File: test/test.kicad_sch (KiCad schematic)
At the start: 0 parts

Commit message: Done with the schematic
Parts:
- added A1: RaspberryPi_Pico, Module:RaspberryPi_Pico_Common_THT, symbol MCU_Module:RaspberryPi_Pico
- added D1, D10, D11, D12, D13, D14, D15, D16, D17, D18, D19, D2, D20, D21, D22, D23, D24, D25, D26, D27, D28, D29, D3, D30, D32, D33, D34, D35, D36, D37, D38, D39, D4, D40, D41, D42, D43, D44, D45, D46, D48, D49, D5, D50, D51, D52, D53, D54, D55, D56, D57, D58, D59, D6, D60, D62, D64, D65, D66, D67, D68, D69, D7, D70, D71, D72, D73, D74, D75, D78, D79, D8, D80, D81, D82, D83, D86, D9, D90, D91, D94, D95, D96: 1N4148, Diode_THT:D_DO-35_SOD27_P7.62mm_Horizontal, symbol Diode:1N4148
- added S1, S2, S3, S4, S5, S6, S7: MX_stab, PCM_marbastlib-mx:STAB_MX_P_2u, symbol PCM_marbastlib-mx:MX_stab
- added SW_0, SW_1, SW_2, SW_3, SW_4, SW_5, SW_6, SW_7, SW_8, SW_9, SW_A1, SW_Apostrophe1, SW_ArrowDown1, SW_ArrowLeft1, SW_ArrowRight1, SW_ArrowUp1, SW_B1, SW_C1, SW_CloseBracket1, SW_Colon1, SW_D1, SW_Del1, SW_E1, SW_ESC1, SW_Equals1, SW_F1, SW_F10, SW_F11, SW_F12, SW_F13, SW_F2, SW_F3, SW_F4, SW_F5, SW_F6, SW_F7, SW_F8, SW_F9, SW_FN1, SW_G1, SW_H1, SW_H2, SW_H3, SW_H4, SW_I1, SW_Insert1, SW_J1, SW_K1, SW_L1, SW_M1, SW_Minus1, SW_N1, SW_O1, SW_OpenBracket1, SW_P1, SW_Q1, SW_R1, SW_S1, SW_Slash1, SW_T1, SW_TILDA1, SW_U1, SW_V+1, SW_V-1, SW_V1, SW_VMute1, SW_W1, SW_X1, SW_Y1, SW_Z1, SW_comma1, SW_dot1: SW_Push, PCM_marbastlib-mx:SW_MX_1u, symbol Switch:SW_Push
- added SW_Alt1, SW_CTRL1, SW_PrintScreen1, SW_Super1: SW_Push, PCM_marbastlib-mx:SW_MX_1.25u, symbol Switch:SW_Push
- added SW_BackSpace1, SW_Enter1, SW_Shift1: SW_Push, PCM_marbastlib-mx:SW_MX_1.75u_STP_1.5, symbol Switch:SW_Push
- added SW_Backslash1, SW_CapsLock1: SW_Push, PCM_marbastlib-mx:SW_MX_1.75u, symbol Switch:SW_Push
- added SW_Space1: SW_Push, PCM_marbastlib-mx:SW_MX_1.75u_STP_1.25, symbol Switch:SW_Push
- added SW_TAB1: SW_Push, PCM_marbastlib-mx:SW_MX_1.5u, symbol Switch:SW_Push
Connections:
- new net: D49.2 (A), SW_CapsLock1.2
- new net: D67.2 (A), SW_X1.2
- new net: D59.2 (A), SW_Colon1.2
- new net: D41.2 (A), SW_I1.2
- new net: D29.2 (A), SW_Equals1.2
- new net: D34.2 (A), SW_Q1.2
- new net: D64.2 (A), SW_H3.2
- new net: D8.2 (A), SW_F7.2
- new net: D20.2 (A), SW_3.2
- new net: D65.2 (A), SW_Shift1.2
- new net: D22.2 (A), SW_5.2
- new net: D14.2 (A), SW_VMute1.2
- new net: D57.2 (A), SW_K1.2
- new net: D13.2 (A), SW_F12.2
- new net: D66.2 (A), SW_Z1.2
- new net: D12.2 (A), SW_F11.2
- new net: D95.2 (A), SW_ArrowDown1.2
- new net: D79.2 (A), SW_ArrowUp1.2
- new net: D5.2 (A), SW_F4.2
- new net: D69.2 (A), SW_V1.2
- new net: D1.2 (A), SW_ESC1.2
- new net: D24.2 (A), SW_7.2
- new net: D11.2 (A), SW_F10.2
- new net: D86.2 (A), SW_Space1.2
- new net: D26.2 (A), SW_9.2
- new net: D75.2 (A), SW_Slash1.2
- new net: D70.2 (A), SW_B1.2
- new net: D25.2 (A), SW_8.2
- new net: D78.2 (A), SW_H1.2
- new net: D81.2 (A), SW_CTRL1.2
- new net: D60.2 (A), SW_Apostrophe1.2
- new net: D4.2 (A), SW_F3.2
- new net: D10.2 (A), SW_F9.2
- new net: D42.2 (A), SW_O1.2
- new net: D43.2 (A), SW_P1.2
- new net: D58.2 (A), SW_L1.2
- new net: D56.2 (A), SW_J1.2
- new net: D48.2 (A), SW_Insert1.2
- new net: D55.2 (A), SW_H4.2
- new net: D7.2 (A), SW_F6.2
- new net: D33.2 (A), SW_TAB1.2
- new net: D91.2 (A), SW_PrintScreen1.2
- new net: D52.2 (A), SW_D1.2
- new net: D28.2 (A), SW_Minus1.2
- new net: D44.2 (A), SW_OpenBracket1.2
- new net: D21.2 (A), SW_4.2
- new net: D53.2 (A), SW_F13.2
- new net: D51.2 (A), SW_S1.2
- new net: D71.2 (A), SW_N1.2
- new net: D80.2 (A), SW_H2.2
- new net: D17.2 (A), SW_TILDA1.2
- new net: D74.2 (A), SW_dot1.2
- new net: D16.2 (A), SW_V+1.2
- new net: D82.2 (A), SW_Super1.2
- new net: D83.2 (A), SW_Alt1.2
- new net: D39.2 (A), SW_Y1.2
- new net: D90.2 (A), SW_FN1.2
- new net: D40.2 (A), SW_U1.2
- new net: D36.2 (A), SW_E1.2
- new net: D94.2 (A), SW_ArrowLeft1.2
- new net: D45.2 (A), SW_CloseBracket1.2
- new net: D2.2 (A), SW_F1.2
- new net: D6.2 (A), SW_F5.2
- new net: D30.2 (A), SW_BackSpace1.2
- new net: D37.2 (A), SW_R1.2
- new net: A1.13 (GND), A1.18 (GND), A1.23 (GND), A1.28 (GND), A1.3 (GND), A1.38 (GND), A1.8 (GND)
- new net: D72.2 (A), SW_M1.2
- new net: D32.2 (A), SW_Del1.2
- new net: D46.2 (A), SW_Backslash1.2
- new net: D15.2 (A), SW_V-1.2
- new net: D54.2 (A), SW_G1.2
- new net: D35.2 (A), SW_W1.2
- new net: D9.2 (A), SW_F8.2
- new net: D62.2 (A), SW_Enter1.2
- new net: D23.2 (A), SW_6.2
- new net: D27.2 (A), SW_0.2
- new net: D68.2 (A), SW_C1.2
- new net: D50.2 (A), SW_A1.2
- new net: D73.2 (A), SW_comma1.2
- new net: D19.2 (A), SW_2.2
- new net: D18.2 (A), SW_1.2
- new net: D38.2 (A), SW_T1.2
- new net: D96.2 (A), SW_ArrowRight1.2
- new net: D3.2 (A), SW_F2.2
- new net Col1: A1.9 (GPIO6), SW_CTRL1.1, SW_CapsLock1.1, SW_ESC1.1, SW_Shift1.1, SW_TAB1.1, SW_TILDA1.1
- new net Col10: A1.20 (GPIO15), SW_9.1, SW_F9.1, SW_FN1.1, SW_L1.1, SW_O1.1, SW_dot1.1
- new net Col11: A1.21 (GPIO16), SW_0.1, SW_Colon1.1, SW_F10.1, SW_P1.1, SW_PrintScreen1.1, SW_Slash1.1
- new net Col12: A1.22 (GPIO17), SW_Apostrophe1.1, SW_F11.1, SW_Minus1.1, SW_OpenBracket1.1
- new net Col13: A1.24 (GPIO18), SW_CloseBracket1.1, SW_Equals1.1, SW_F12.1
- new net Col14: A1.25 (GPIO19), SW_ArrowLeft1.1, SW_BackSpace1.1, SW_Backslash1.1, SW_Enter1.1, SW_H1.1, SW_VMute1.1
- new net Col15: A1.26 (GPIO20), SW_ArrowDown1.1, SW_ArrowUp1.1, SW_V-1.1
- new net Col16: A1.27 (GPIO21), SW_ArrowRight1.1, SW_Del1.1, SW_H2.1, SW_H3.1, SW_Insert1.1, SW_V+1.1
- new net Col2: A1.10 (GPIO7), SW_1.1, SW_A1.1, SW_F1.1, SW_Q1.1, SW_Super1.1, SW_Z1.1
- new net Col3: A1.11 (GPIO8), SW_2.1, SW_Alt1.1, SW_F2.1, SW_S1.1, SW_W1.1, SW_X1.1
- new net Col4: A1.12 (GPIO9), SW_3.1, SW_C1.1, SW_D1.1, SW_E1.1, SW_F3.1
- new net Col5: A1.14 (GPIO10), SW_4.1, SW_F13.1, SW_F4.1, SW_R1.1, SW_V1.1
- new net Col6: A1.15 (GPIO11), SW_5.1, SW_B1.1, SW_F5.1, SW_G1.1, SW_Space1.1, SW_T1.1
- new net Col7: A1.16 (GPIO12), SW_6.1, SW_F6.1, SW_H4.1, SW_N1.1, SW_Y1.1
- new net Col8: A1.17 (GPIO13), SW_7.1, SW_F7.1, SW_J1.1, SW_M1.1, SW_U1.1
- new net Col9: A1.19 (GPIO14), SW_8.1, SW_F8.1, SW_I1.1, SW_K1.1, SW_comma1.1
- new net Row1: A1.1 (GPIO0), D1.1 (K), D10.1 (K), D11.1 (K), D12.1 (K), D13.1 (K), D14.1 (K), D15.1 (K), D16.1 (K), D2.1 (K), D3.1 (K), D4.1 (K), D5.1 (K), D6.1 (K), D7.1 (K), D8.1 (K), D9.1 (K)
- new net Row2: A1.2 (GPIO1), D17.1 (K), D18.1 (K), D19.1 (K), D20.1 (K), D21.1 (K), D22.1 (K), D23.1 (K), D24.1 (K), D25.1 (K), D26.1 (K), D27.1 (K), D28.1 (K), D29.1 (K), D30.1 (K), D32.1 (K)
- new net Row3: A1.4 (GPIO2), D33.1 (K), D34.1 (K), D35.1 (K), D36.1 (K), D37.1 (K), D38.1 (K), D39.1 (K), D40.1 (K), D41.1 (K), D42.1 (K), D43.1 (K), D44.1 (K), D45.1 (K), D46.1 (K), D48.1 (K)
- new net Row4: A1.5 (GPIO3), D49.1 (K), D50.1 (K), D51.1 (K), D52.1 (K), D53.1 (K), D54.1 (K), D55.1 (K), D56.1 (K), D57.1 (K), D58.1 (K), D59.1 (K), D60.1 (K), D62.1 (K), D64.1 (K)
- new net Row5: A1.6 (GPIO4), D65.1 (K), D66.1 (K), D67.1 (K), D68.1 (K), D69.1 (K), D70.1 (K), D71.1 (K), D72.1 (K), D73.1 (K), D74.1 (K), D75.1 (K), D78.1 (K), D79.1 (K), D80.1 (K)
- new net Row6: A1.7 (GPIO5), D81.1 (K), D82.1 (K), D83.1 (K), D86.1 (K), D90.1 (K), D91.1 (K), D94.1 (K), D95.1 (K), D96.1 (K)

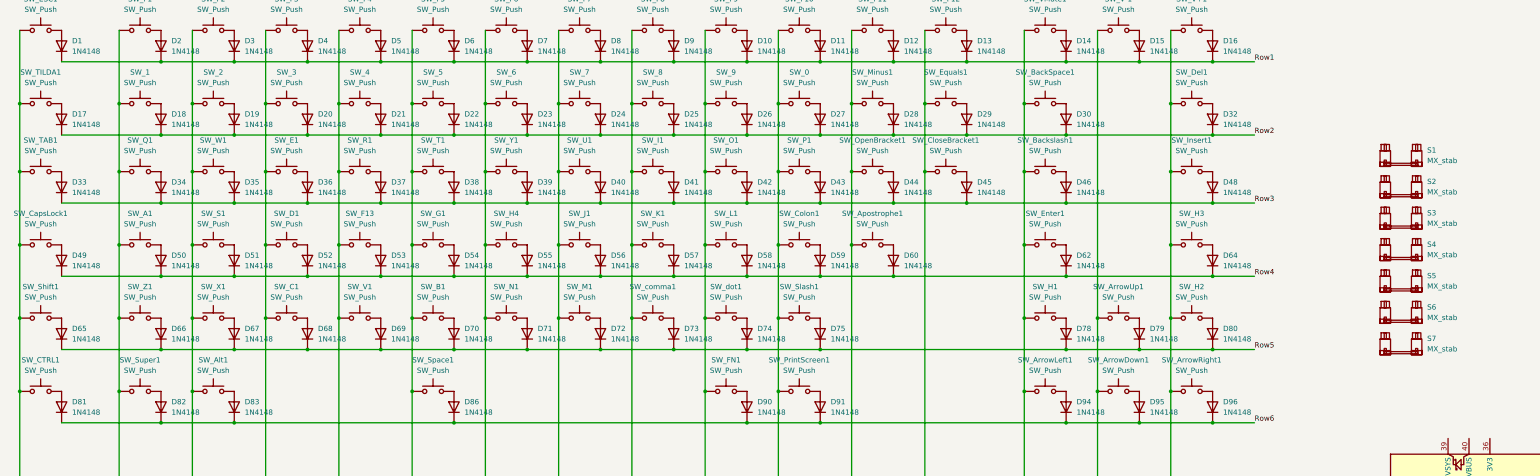
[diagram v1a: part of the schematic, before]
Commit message: added layout using keyboard-layout-editor
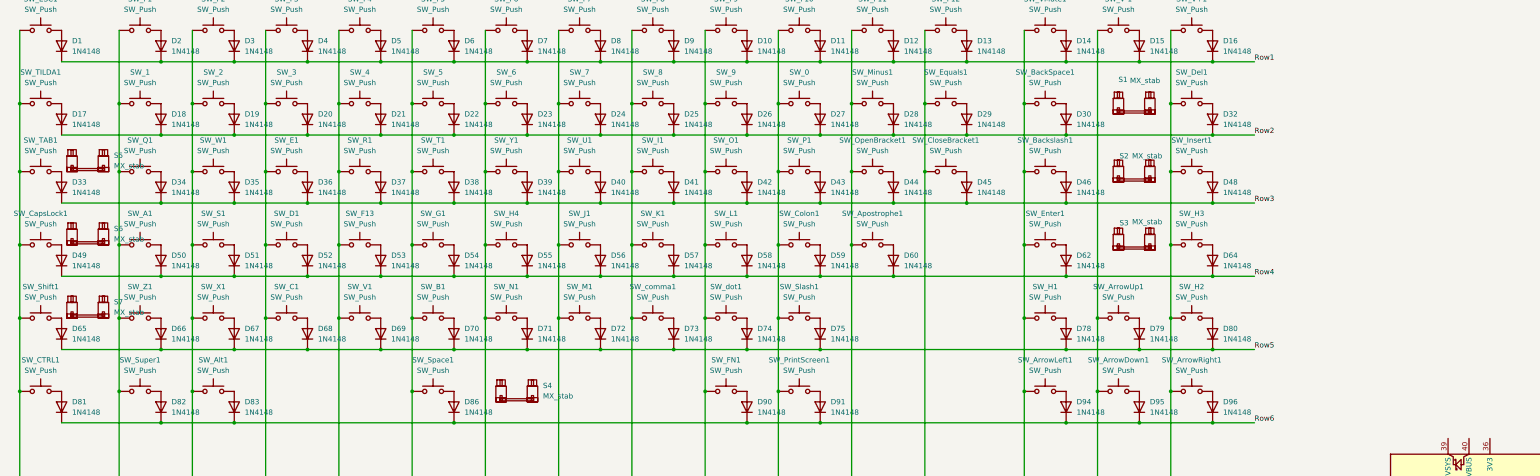
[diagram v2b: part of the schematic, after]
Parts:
- S1, S2, S3, S4, S5, S6, S7: footprint PCM_marbastlib-mx:STAB_MX_P_2u -> PCM_marbastlib-mx:SW_MX_1u
- SW_Alt1, SW_CTRL1, SW_PrintScreen1, SW_Super1: footprint PCM_marbastlib-mx:SW_MX_1.25u -> PCM_marbastlib-mx:SW_MX_1u
- SW_BackSpace1, SW_Enter1, SW_Shift1: footprint PCM_marbastlib-mx:SW_MX_1.75u_STP_1.5 -> PCM_marbastlib-mx:SW_MX_1u
- SW_Backslash1, SW_CapsLock1: footprint PCM_marbastlib-mx:SW_MX_1.75u -> PCM_marbastlib-mx:SW_MX_1u
- SW_Space1: footprint PCM_marbastlib-mx:SW_MX_1.75u_STP_1.25 -> PCM_marbastlib-mx:SW_MX_1u
- SW_TAB1: footprint PCM_marbastlib-mx:SW_MX_1.5u -> PCM_marbastlib-mx:SW_MX_1u
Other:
- moved on the sheet: S1, S2, S3, S4, S5, S6, S7
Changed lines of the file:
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@@
 	(symbol
 		(lib_id "PCM_marbastlib-mx:MX_stab")
-		(at 355.6 107.95 0)
+		(at 290.83 104.14 0)
 		(unit 1)
 		(body_style 1)
@@
 		(in_pos_files yes)
 		(dnp no)
-		(fields_autoplaced yes)
 		(property "Reference" "S2"
-			(at 361.95 106.5529 0)
+			(at 287.274 100.33 0)
 			(show_name no)
 			(do_not_autoplace no)
@@
 		)
 		(property "Value" "MX_stab"
-			(at 361.95 109.0929 0)
+			(at 290.322 100.33 0)
 			(show_name no)
 			(do_not_autoplace no)
@@
 			)
 		)
-		(property "Footprint" "PCM_marbastlib-mx:STAB_MX_P_2u"
-			(at 355.6 107.95 0)
+		(property "Footprint" "PCM_marbastlib-mx:SW_MX_1u"
+			(at 290.83 104.14 0)
 			(hide yes)
 			(show_name no)
@@
 		)
 		(property "Datasheet" ""
-			(at 355.6 107.95 0)
+			(at 290.83 104.14 0)
 			(hide yes)
 			(show_name no)
@@
 		)
 		(property "Description" "Cherry MX-style stabilizer"
-			(at 355.6 107.95 0)
+			(at 290.83 104.14 0)
 			(hide yes)
 			(show_name no)
@@
 			)
 		)
-		(property "Footprint" "PCM_marbastlib-mx:SW_MX_1.75u_STP_1.25"
+		(property "Footprint" "PCM_marbastlib-mx:SW_MX_1u"
 			(at 120.65 152.4 0)
 			(hide yes)
@@
 	(symbol
 		(lib_id "PCM_marbastlib-mx:MX_stab")
-		(at 355.6 100.33 0)
+		(at 290.83 87.63 0)
 		(unit 1)
 		(body_style 1)
@@
 		(in_pos_files yes)
 		(dnp no)
-		(fields_autoplaced yes)
 		(property "Reference" "S1"
-			(at 361.95 98.9329 0)
+			(at 287.02 81.788 0)
 			(show_name no)
 			(do_not_autoplace no)
@@
 		)
 		(property "Value" "MX_stab"
-			(at 361.95 101.4729 0)
+			(at 289.814 82.042 0)
 			(show_name no)
 			(do_not_autoplace no)
@@
 			)
 		)
-		(property "Footprint" "PCM_marbastlib-mx:STAB_MX_P_2u"
-			(at 355.6 100.33 0)
+		(property "Footprint" "PCM_marbastlib-mx:SW_MX_1u"
+			(at 290.83 87.63 0)
 			(hide yes)
 			(show_name no)
@@
 		)
 		(property "Datasheet" ""
-			(at 355.6 100.33 0)
+			(at 290.83 87.63 0)
 			(hide yes)
 			(show_name no)
@@
 		)
 		(property "Description" "Cherry MX-style stabilizer"
-			(at 355.6 100.33 0)
+			(at 290.83 87.63 0)
 			(hide yes)
 			(show_name no)
@@
 			)
 		)
-		(property "Footprint" "PCM_marbastlib-mx:SW_MX_1.75u"
+		(property "Footprint" "PCM_marbastlib-mx:SW_MX_1u"
 			(at 25.4 116.84 0)
 			(hide yes)
@@
 			)
 		)
-		(property "Footprint" "PCM_marbastlib-mx:SW_MX_1.5u"
+		(property "Footprint" "PCM_marbastlib-mx:SW_MX_1u"
 			(at 25.4 99.06 0)
 			(hide yes)
@@
 	(symbol
 		(lib_id "PCM_marbastlib-mx:MX_stab")
-		(at 355.6 138.43 0)
+		(at 36.83 119.38 0)
 		(unit 1)
 		(body_style 1)
@@
 		(fields_autoplaced yes)
 		(property "Reference" "S6"
-			(at 361.95 137.0329 0)
+			(at 43.18 117.9829 0)
 			(show_name no)
 			(do_not_autoplace no)
@@
 		)
 		(property "Value" "MX_stab"
-			(at 361.95 139.5729 0)
+			(at 43.18 120.5229 0)
 			(show_name no)
 			(do_not_autoplace no)
@@
 			)
 		)
-		(property "Footprint" "PCM_marbastlib-mx:STAB_MX_P_2u"
-			(at 355.6 138.43 0)
+		(property "Footprint" "PCM_marbastlib-mx:SW_MX_1u"
+			(at 36.83 119.38 0)
 			(hide yes)
 			(show_name no)
@@
 		)
 		(property "Datasheet" ""
-			(at 355.6 138.43 0)
+			(at 36.83 119.38 0)
 			(hide yes)
 			(show_name no)
@@
 		)
 		(property "Description" "Cherry MX-style stabilizer"
-			(at 355.6 138.43 0)
+			(at 36.83 119.38 0)
 			(hide yes)
 			(show_name no)
@@
 	(symbol
 		(lib_id "PCM_marbastlib-mx:MX_stab")
-		(at 355.6 130.81 0)
+		(at 36.83 101.6 0)
 		(unit 1)
 		(body_style 1)
@@
 		(fields_autoplaced yes)
 		(property "Reference" "S5"
-			(at 361.95 129.4129 0)
+			(at 43.18 100.2029 0)
 			(show_name no)
 			(do_not_autoplace no)
@@
 		)
 		(property "Value" "MX_stab"
-			(at 361.95 131.9529 0)
+			(at 43.18 102.7429 0)
 			(show_name no)
 			(do_not_autoplace no)
@@
 			)
 		)
-		(property "Footprint" "PCM_marbastlib-mx:STAB_MX_P_2u"
-			(at 355.6 130.81 0)
+		(property "Footprint" "PCM_marbastlib-mx:SW_MX_1u"
+			(at 36.83 101.6 0)
 			(hide yes)
 			(show_name no)
@@
 		)
 		(property "Datasheet" ""
-			(at 355.6 130.81 0)
+			(at 36.83 101.6 0)
 			(hide yes)
 			(show_name no)
@@
 		)
 		(property "Description" "Cherry MX-style stabilizer"
-			(at 355.6 130.81 0)
+			(at 36.83 101.6 0)
 			(hide yes)
 			(show_name no)
@@
 	(symbol
 		(lib_id "PCM_marbastlib-mx:MX_stab")
-		(at 355.6 115.57 0)
+		(at 290.83 120.65 0)
 		(unit 1)
 		(body_style 1)
@@
 		(in_pos_files yes)
 		(dnp no)
-		(fields_autoplaced yes)
 		(property "Reference" "S3"
-			(at 361.95 114.1729 0)
+			(at 287.274 116.586 0)
 			(show_name no)
 			(do_not_autoplace no)
@@
 		)
 		(property "Value" "MX_stab"
-			(at 361.95 116.7129 0)
+			(at 290.322 116.332 0)
 			(show_name no)
 			(do_not_autoplace no)
@@
 			)
 		)
-		(property "Footprint" "PCM_marbastlib-mx:STAB_MX_P_2u"
-			(at 355.6 115.57 0)
+		(property "Footprint" "PCM_marbastlib-mx:SW_MX_1u"
+			(at 290.83 120.65 0)
 			(hide yes)
 			(show_name no)
@@
 		)
 		(property "Datasheet" ""
-			(at 355.6 115.57 0)
+			(at 290.83 120.65 0)
 			(hide yes)
 			(show_name no)
@@
 		)
 		(property "Description" "Cherry MX-style stabilizer"
-			(at 355.6 115.57 0)
+			(at 290.83 120.65 0)
 			(hide yes)
 			(show_name no)
@@
 			)
 		)
-		(property "Footprint" "PCM_marbastlib-mx:SW_MX_1.75u"
+		(property "Footprint" "PCM_marbastlib-mx:SW_MX_1u"
 			(at 269.24 99.06 0)
 			(hide yes)
@@
 			)
 		)
-		(property "Footprint" "PCM_marbastlib-mx:SW_MX_1.25u"
+		(property "Footprint" "PCM_marbastlib-mx:SW_MX_1u"
 			(at 209.55 152.4 0)
 			(hide yes)
@@
 			)
 		)
-		(property "Footprint" "PCM_marbastlib-mx:SW_MX_1.75u_STP_1.5"
+		(property "Footprint" "PCM_marbastlib-mx:SW_MX_1u"
 			(at 25.4 134.62 0)
 			(hide yes)
@@
 			)
 		)
-		(property "Footprint" "PCM_marbastlib-mx:SW_MX_1.25u"
+		(property "Footprint" "PCM_marbastlib-mx:SW_MX_1u"
 			(at 49.53 152.4 0)
 			(hide yes)
@@
 	(symbol
 		(lib_id "PCM_marbastlib-mx:MX_stab")
-		(at 355.6 146.05 0)
+		(at 36.83 137.16 0)
 		(unit 1)
 		(body_style 1)
@@
 		(fields_autoplaced yes)
 		(property "Reference" "S7"
-			(at 361.95 144.6529 0)
+			(at 43.18 135.7629 0)
 			(show_name no)
 			(do_not_autoplace no)
@@
 		)
 		(property "Value" "MX_stab"
-			(at 361.95 147.1929 0)
+			(at 43.18 138.3029 0)
 			(show_name no)
 			(do_not_autoplace no)
@@
 			)
 		)
-		(property "Footprint" "PCM_marbastlib-mx:STAB_MX_P_2u"
-			(at 355.6 146.05 0)
+		(property "Footprint" "PCM_marbastlib-mx:SW_MX_1u"
+			(at 36.83 137.16 0)
 			(hide yes)
 			(show_name no)
@@
 		)
 		(property "Datasheet" ""
-			(at 355.6 146.05 0)
+			(at 36.83 137.16 0)
 			(hide yes)
 			(show_name no)
@@
 		)
 		(property "Description" "Cherry MX-style stabilizer"
-			(at 355.6 146.05 0)
+			(at 36.83 137.16 0)
 			(hide yes)
 			(show_name no)
@@
 	(symbol
 		(lib_id "PCM_marbastlib-mx:MX_stab")
-		(at 355.6 123.19 0)
+		(at 140.97 157.48 0)
 		(unit 1)
 		(body_style 1)
@@
 		(fields_autoplaced yes)
 		(property "Reference" "S4"
-			(at 361.95 121.7929 0)
+			(at 147.32 156.0829 0)
 			(show_name no)
 			(do_not_autoplace no)
@@
 		)
 		(property "Value" "MX_stab"
-			(at 361.95 124.3329 0)
+			(at 147.32 158.6229 0)
 			(show_name no)
 			(do_not_autoplace no)
@@
 			)
 		)
-		(property "Footprint" "PCM_marbastlib-mx:STAB_MX_P_2u"
-			(at 355.6 123.19 0)
+		(property "Footprint" "PCM_marbastlib-mx:SW_MX_1u"
+			(at 140.97 157.48 0)
 			(hide yes)
 			(show_name no)
@@
 		)
 		(property "Datasheet" ""
-			(at 355.6 123.19 0)
+			(at 140.97 157.48 0)
 			(hide yes)
 			(show_name no)
@@
 		)
 		(property "Description" "Cherry MX-style stabilizer"
-			(at 355.6 123.19 0)
+			(at 140.97 157.48 0)
 			(hide yes)
 			(show_name no)
@@
 			)
 		)
-		(property "Footprint" "PCM_marbastlib-mx:SW_MX_1.75u_STP_1.5"
+		(property "Footprint" "PCM_marbastlib-mx:SW_MX_1u"
 			(at 269.24 82.55 0)
 			(hide yes)
@@
 			)
 		)
-		(property "Footprint" "PCM_marbastlib-mx:SW_MX_1.25u"
+		(property "Footprint" "PCM_marbastlib-mx:SW_MX_1u"
 			(at 67.31 152.4 0)
 			(hide yes)
@@
 			)
 		)
-		(property "Footprint" "PCM_marbastlib-mx:SW_MX_1.75u_STP_1.5"
+		(property "Footprint" "PCM_marbastlib-mx:SW_MX_1u"
 			(at 269.24 116.84 0)
 			(hide yes)
@@
 			)
 		)
-		(property "Footprint" "PCM_marbastlib-mx:SW_MX_1.25u"
+		(property "Footprint" "PCM_marbastlib-mx:SW_MX_1u"
 			(at 25.4 152.4 0)
 			(hide yes)

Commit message: Started pcb editor
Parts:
- removed S2, S5, S6: MX_stab, PCM_marbastlib-mx:SW_MX_1u, symbol PCM_marbastlib-mx:MX_stab
- added D81: 1N4148, Diode_THT:D_DO-35_SOD27_P7.62mm_Horizontal, symbol Diode:1N4148
- added SW81: SW_Push, PCM_marbastlib-mx:SW_MX_1u, symbol Switch:SW_Push
- S1: footprint PCM_marbastlib-mx:SW_MX_1u -> PCM_marbastlib-mx:STAB_MX_2u
- S2: renamed from S3; footprint PCM_marbastlib-mx:SW_MX_1u -> PCM_marbastlib-mx:STAB_MX_2.25u
- S3: renamed from S7; footprint PCM_marbastlib-mx:SW_MX_1u -> PCM_marbastlib-mx:STAB_MX_2.25u
- S4: footprint PCM_marbastlib-mx:SW_MX_1u -> PCM_marbastlib-mx:STAB_MX_5u
- renumbered D32 to D31, D33 to D32, D34 to D33, D35 to D34, D36 to D35, D37 to D36, D38 to D37, D39 to D38, D40 to D39, D41 to D40, D42 to D41, D43 to D42, D44 to D43, D45 to D44, D46 to D45, D48 to D46, D49 to D47, D50 to D48, D51 to D49, D52 to D50, D53 to D51, D54 to D52, D55 to D53, D56 to D54, D57 to D55, D58 to D56, D59 to D57, D60 to D58, D62 to D59, D64 to D60, D65 to D61, D66 to D62, D67 to D63, D68 to D64, D69 to D65, D70 to D66, D71 to D67, D72 to D68, D73 to D69, D74 to D70, D75 to D71, D78 to D72, D79 to D73, D80 to D74, D81 to D75, D82 to D76, D83 to D77, D86 to D78, D90 to D79, D91 to D80, D94 to D82, D95 to D83, D96 to D84, SW_ESC1 to SW1, SW_F9 to SW10, SW_F10 to SW11, SW_F11 to SW12, SW_F12 to SW13, SW_VMute1 to SW14, SW_V-1 to SW15, SW_V+1 to SW16, SW_TILDA1 to SW17, SW_1 to SW18, SW_2 to SW19, SW_F1 to SW2, SW_3 to SW20, SW_4 to SW21, SW_5 to SW22, SW_6 to SW23, SW_7 to SW24, SW_8 to SW25, SW_9 to SW26, SW_0 to SW27, SW_Minus1 to SW28, SW_Equals1 to SW29, SW_F2 to SW3, SW_BackSpace1 to SW30, SW_Del1 to SW31, SW_TAB1 to SW32, SW_Q1 to SW33, SW_W1 to SW34, SW_E1 to SW35, SW_R1 to SW36, SW_T1 to SW37, SW_Y1 to SW38, SW_U1 to SW39, SW_F3 to SW4, SW_I1 to SW40, SW_O1 to SW41, SW_P1 to SW42, SW_OpenBracket1 to SW43, SW_CloseBracket1 to SW44, SW_Backslash1 to SW45, SW_Insert1 to SW46, SW_CapsLock1 to SW47, SW_A1 to SW48, SW_S1 to SW49, SW_F4 to SW5, SW_D1 to SW50, SW_F13 to SW51, SW_G1 to SW52, SW_H4 to SW53, SW_J1 to SW54, SW_K1 to SW55, SW_L1 to SW56, SW_Colon1 to SW57, SW_Apostrophe1 to SW58, SW_Enter1 to SW59, SW_F5 to SW6, SW_H3 to SW60, SW_Shift1 to SW61, SW_Z1 to SW62, SW_X1 to SW63, SW_C1 to SW64, SW_V1 to SW65, SW_B1 to SW66, SW_N1 to SW67, SW_M1 to SW68, SW_comma1 to SW69, SW_F6 to SW7, SW_dot1 to SW70, SW_Slash1 to SW71, SW_H1 to SW72, SW_ArrowUp1 to SW73, SW_H2 to SW74, SW_CTRL1 to SW75, SW_Super1 to SW76, SW_Alt1 to SW77, SW_Space1 to SW78, SW_FN1 to SW79, SW_F7 to SW8, SW_PrintScreen1 to SW80, SW_ArrowLeft1 to SW82, SW_ArrowDown1 to SW83, SW_ArrowRight1 to SW84, SW_F8 to SW9
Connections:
- net Col12: now also SW81.1
- net Row6: now also D81.1 (K)
- new net: D81.2 (A), SW81.2

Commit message: Finished the pcb design
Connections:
- net Col1: now also A1.1 (GPIO0); no longer A1.9 (GPIO6)
- net Col10: now also A1.12 (GPIO9), SW80.1; no longer A1.20 (GPIO15), SW79.1
- net Col11: now also A1.14 (GPIO10), SW81.1; no longer A1.21 (GPIO16), SW80.1
- net Col12: now also A1.15 (GPIO11); no longer A1.22 (GPIO17), SW81.1
- net Col13: now also A1.16 (GPIO12); no longer A1.24 (GPIO18)
- net Col14: now also A1.17 (GPIO13); no longer A1.25 (GPIO19)
- net Col15: now also A1.19 (GPIO14); no longer A1.26 (GPIO20)
- net Col16: now also A1.20 (GPIO15); no longer A1.27 (GPIO21)
- net Col2: now also A1.2 (GPIO1); no longer A1.10 (GPIO7)
- net Col3: now also A1.4 (GPIO2); no longer A1.11 (GPIO8)
- net Col4: now also A1.5 (GPIO3); no longer A1.12 (GPIO9)
- net Col5: now also A1.6 (GPIO4); no longer A1.14 (GPIO10)
- net Col6: now also A1.7 (GPIO5); no longer A1.15 (GPIO11)
- net Col7: now also A1.9 (GPIO6); no longer A1.16 (GPIO12)
- net Col8: now also A1.10 (GPIO7); no longer A1.17 (GPIO13)
- net Col9: now also A1.11 (GPIO8), SW79.1; no longer A1.19 (GPIO14)
- net Row1: now also A1.22 (GPIO17); no longer A1.1 (GPIO0)
- net Row2: now also A1.24 (GPIO18); no longer A1.2 (GPIO1)
- net Row3: now also A1.25 (GPIO19); no longer A1.4 (GPIO2)
- net Row4: now also A1.26 (GPIO20); no longer A1.5 (GPIO3)
- net Row5: now also A1.27 (GPIO21); no longer A1.6 (GPIO4)
- net Row6: now also A1.29 (GPIO22); no longer A1.7 (GPIO5)
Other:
- moved on the sheet: A1, D1, D10, D11, D12, D13, D14, D15, D16, D17, D18, D19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
